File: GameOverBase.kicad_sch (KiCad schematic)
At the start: 49 parts, among them J1 USB_C_DEALON-USB-US31-106, J2 Serial Port, J3 add-on conn, Q1 PMN48XP, SW1 SW_DIP_x08, SW2 boot, SW3 Reset, U1 ESP32-WROOM-E, U2 4021, U3 MCP73831-2ACI-OT, U4 XC6210B332MR

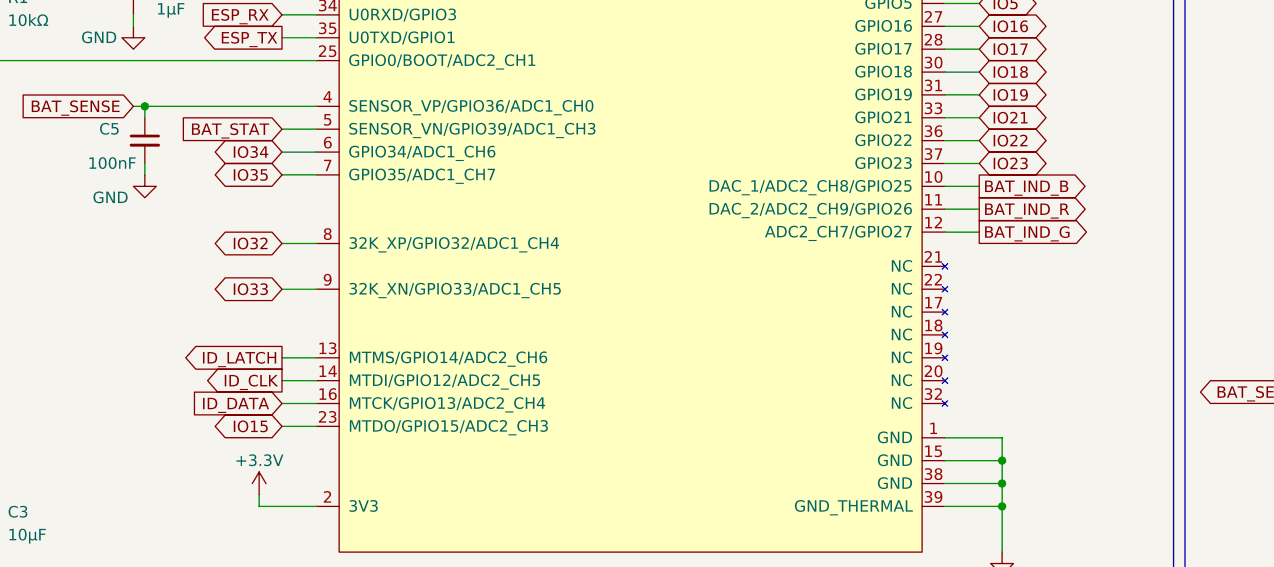
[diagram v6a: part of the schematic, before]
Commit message: Brings in DIP switches
To route this I needed to swap around the pins on the latch and clock
lines for the 4021 and also the RGB led.
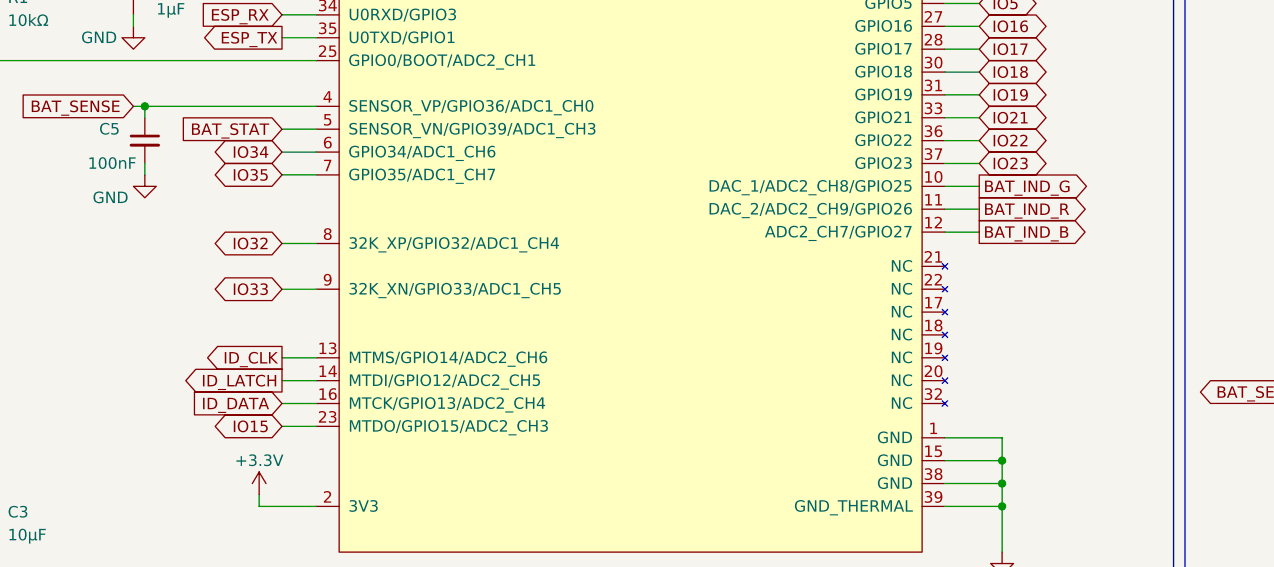
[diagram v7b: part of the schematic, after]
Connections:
- net BAT_IND_B: now also U1.12 (ADC2_CH7/GPIO27); no longer U1.10 (DAC_1/ADC2_CH8/GPIO25)
- net BAT_IND_G: now also U1.10 (DAC_1/ADC2_CH8/GPIO25); no longer U1.12 (ADC2_CH7/GPIO27)
- net ID_CLK: now also U1.13 (MTMS/GPIO14/ADC2_CH6); no longer U1.14 (MTDI/GPIO12/ADC2_CH5)
- net ID_LATCH: now also U1.14 (MTDI/GPIO12/ADC2_CH5); no longer U1.13 (MTMS/GPIO14/ADC2_CH6)
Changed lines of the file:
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@@
     )
   )
-  (global_label "ID_CLK" (shape output) (at 62.23 90.17 180) (fields_autoplaced)
-    (effects (font (size 1.27 1.27)) (justify right))
-    (property "Intersheetrefs" "${INTERSHEET_REFS}" (id 0) (at 53.0725 90.17 0)
+  (global_label "ID_CLK" (shape output) (at 62.23 87.63 180) (fields_autoplaced)
+    (effects (font (size 1.27 1.27)) (justify right))
+    (property "Intersheetrefs" "${INTERSHEET_REFS}" (id 0) (at 53.0725 87.63 0)
       (effects (font (size 1.27 1.27)) (justify right) hide)
     )
@@
     )
   )
-  (global_label "ID_LATCH" (shape output) (at 62.23 87.63 180) (fields_autoplaced)
-    (effects (font (size 1.27 1.27)) (justify right))
-    (property "Intersheetrefs" "${INTERSHEET_REFS}" (id 0) (at 50.9558 87.63 0)
+  (global_label "ID_LATCH" (shape output) (at 62.23 90.17 180) (fields_autoplaced)
+    (effects (font (size 1.27 1.27)) (justify right))
+    (property "Intersheetrefs" "${INTERSHEET_REFS}" (id 0) (at 50.9558 90.17 0)
       (effects (font (size 1.27 1.27)) (justify right) hide)
     )
@@
     )
   )
-  (global_label "BAT_IND_G" (shape output) (at 139.7 73.66 0) (fields_autoplaced)
+  (global_label "BAT_IND_G" (shape output) (at 139.7 68.58 0) (fields_autoplaced)
+    (effects (font (size 1.27 1.27)) (justify left))
+    (property "Intersheetrefs" "${INTERSHEET_REFS}" (id 0) (at 152.1837 68.58 0)
+      (effects (font (size 1.27 1.27)) (justify left) hide)
+    )
+  )
+  (global_label "IO17" (shape bidirectional) (at 91.44 161.29 180) (fields_autoplaced)
+    (effects (font (size 1.27 1.27)) (justify right))
+    (property "Intersheetrefs" "${INTERSHEET_REFS}" (id 0) (at 83.2274 161.29 0)
+      (effects (font (size 1.27 1.27)) (justify right) hide)
+    )
+  )
+  (global_label "IO34" (shape bidirectional) (at 62.23 64.77 180) (fields_autoplaced)
+    (effects (font (size 1.27 1.27)) (justify right))
+    (property "Intersheetrefs" "${INTERSHEET_REFS}" (id 0) (at 54.0174 64.77 0)
+      (effects (font (size 1.27 1.27)) (justify right) hide)
+    )
+  )
+  (global_label "ESP_BOOT" (shape input) (at 59.69 185.42 0) (fields_autoplaced)
+    (effects (font (size 1.27 1.27)) (justify left))
+    (property "Intersheetrefs" "${INTERSHEET_REFS}" (id 0) (at 71.9317 185.42 0)
+      (effects (font (size 1.27 1.27)) (justify left) hide)
+    )
+  )
+  (global_label "BAT_IND_B" (shape output) (at 139.7 73.66 0) (fields_autoplaced)
     (effects (font (size 1.27 1.27)) (justify left))
     (property "Intersheetrefs" "${INTERSHEET_REFS}" (id 0) (at 152.1837 73.66 0)
       (effects (font (size 1.27 1.27)) (justify left) hide)
     )
-  )
-  (global_label "IO17" (shape bidirectional) (at 91.44 161.29 180) (fields_autoplaced)
-    (effects (font (size 1.27 1.27)) (justify right))
-    (property "Intersheetrefs" "${INTERSHEET_REFS}" (id 0) (at 83.2274 161.29 0)
-      (effects (font (size 1.27 1.27)) (justify right) hide)
-    )
-  )
-  (global_label "IO34" (shape bidirectional) (at 62.23 64.77 180) (fields_autoplaced)
-    (effects (font (size 1.27 1.27)) (justify right))
-    (property "Intersheetrefs" "${INTERSHEET_REFS}" (id 0) (at 54.0174 64.77 0)
-      (effects (font (size 1.27 1.27)) (justify right) hide)
-    )
-  )
-  (global_label "ESP_BOOT" (shape input) (at 59.69 185.42 0) (fields_autoplaced)
-    (effects (font (size 1.27 1.27)) (justify left))
-    (property "Intersheetrefs" "${INTERSHEET_REFS}" (id 0) (at 71.9317 185.42 0)
-      (effects (font (size 1.27 1.27)) (justify left) hide)
-    )
-  )
-  (global_label "BAT_IND_B" (shape output) (at 139.7 68.58 0) (fields_autoplaced)
-    (effects (font (size 1.27 1.27)) (justify left))
-    (property "Intersheetrefs" "${INTERSHEET_REFS}" (id 0) (at 152.1837 68.58 0)
-      (effects (font (size 1.27 1.27)) (justify left) hide)
-    )
